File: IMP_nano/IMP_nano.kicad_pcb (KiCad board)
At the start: 2 copper layers, 34 parts, among them J1 KF301, J2 Holes, Q1 BC847, Q2 AO3400A, SW1 SW_DPST_x2, SW2 SW_DIP_x04, U1 STM32L051C8T6

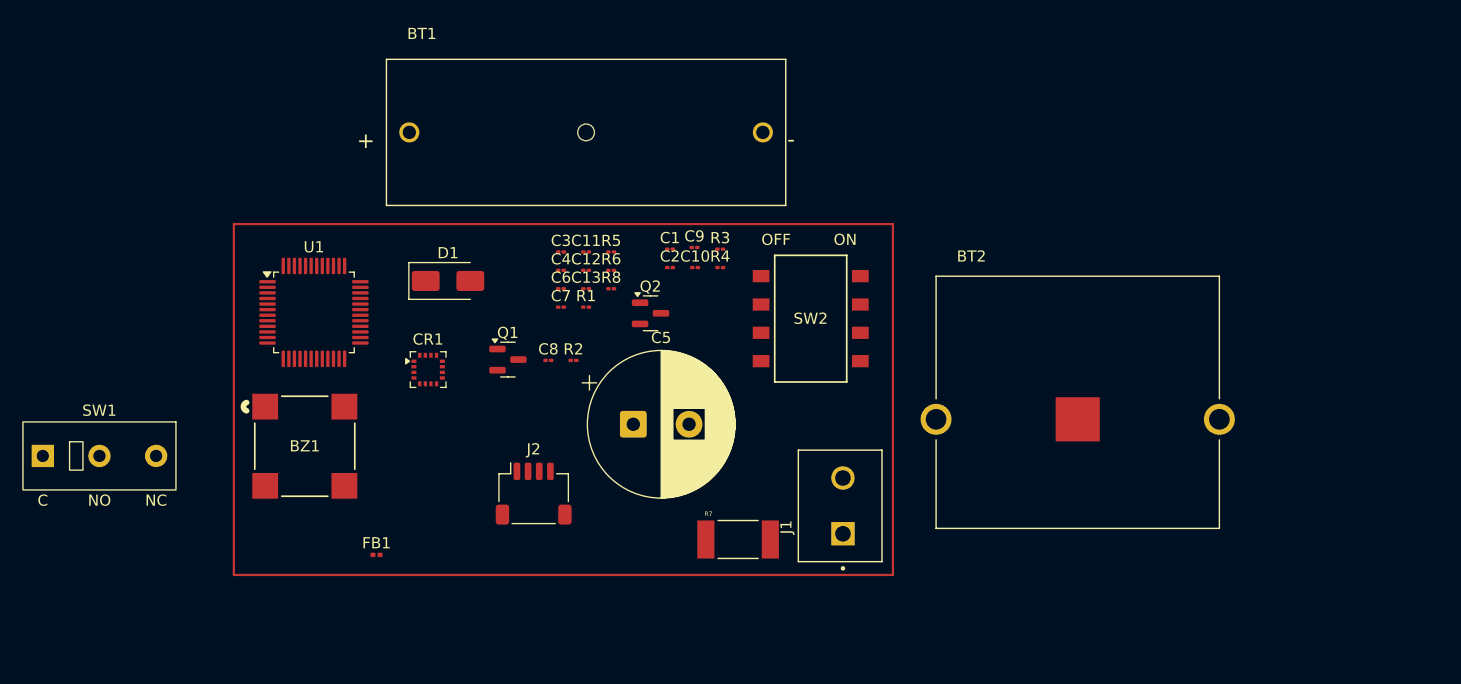
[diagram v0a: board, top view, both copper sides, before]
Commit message: precomplete of back side of pcb
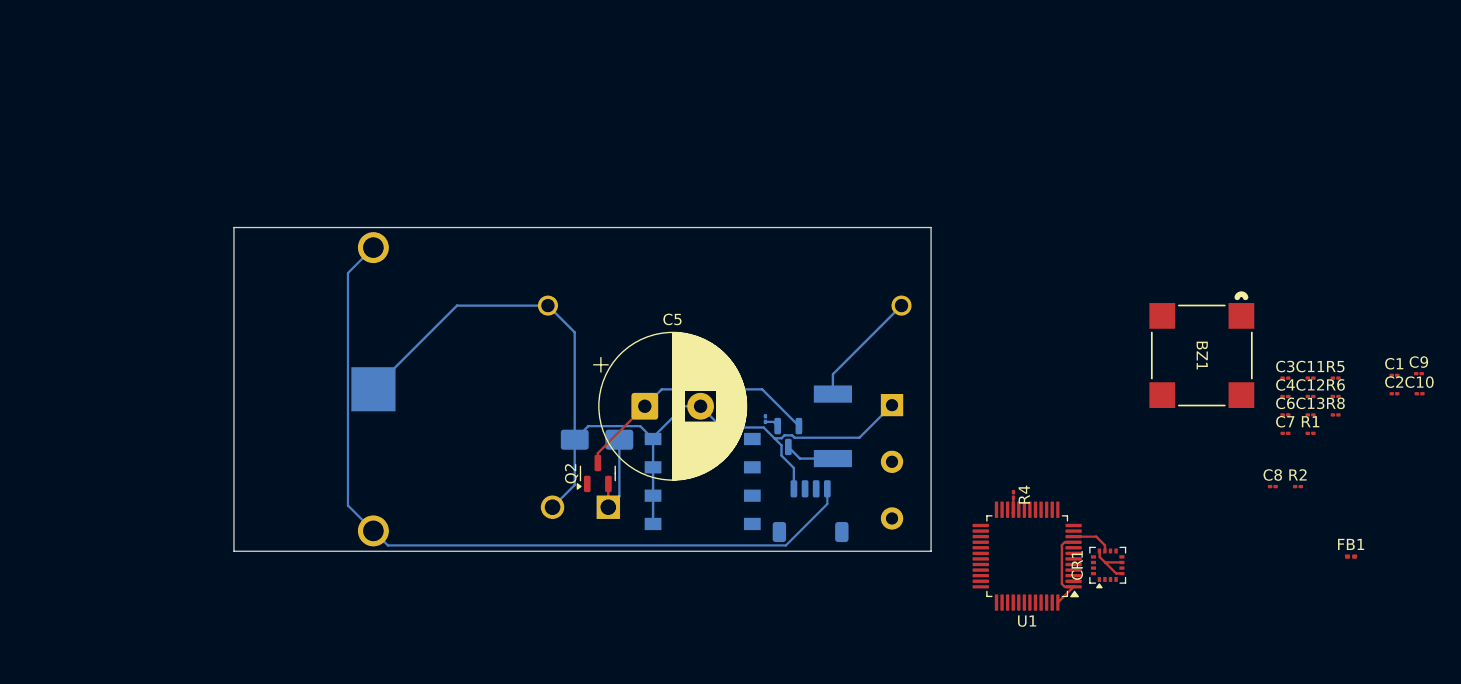
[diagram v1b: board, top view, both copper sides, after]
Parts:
- BT1, BT2, D1, J1, J2, Q1, R3, R7, SW1, SW2: moved to B.Cu
- moved FB1 87.4 mm to (193.7, 106.0)
- moved BZ1 80.8 mm to (180.3, 88.0), turned to -90 degrees
- moved SW1 76.3 mm to (152.5, 92.4), turned to -90 degrees
- moved U1 67.6 mm to (164.6, 106.0), turned to 180 degrees
- moved C1 65.9 mm to (197.6, 89.8)
- moved C10 65.9 mm to (199.8, 91.4)
- moved C11 65.9 mm to (190.0, 90.0)
- moved C12 65.9 mm to (190.0, 91.7)
- moved C13 65.9 mm to (190.0, 93.3)
- moved C2 65.9 mm to (197.6, 91.4)
- moved C3 65.9 mm to (187.8, 90.0)
- moved C4 65.9 mm to (187.8, 91.7)
- moved C6 65.9 mm to (187.8, 93.3)
- moved C7 65.9 mm to (187.8, 95.0)
- moved C8 65.9 mm to (186.6, 99.7)
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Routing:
- net GND: track 0.00 -> 89.6 mm
- net +3.3V: track 0.00 -> 79.2 mm
- net Net-(Q1-E): track 0.00 -> 22.6 mm
- net +12V: track 0.00 -> 10.5 mm
- net Net-(D1-K): track 0.00 -> 8.17 mm
- net Net-(Q1-C): track 0.00 -> 4.43 mm
- net GPIO_WKP: track 0.00 -> 3.64 mm
- net Activate: track 0.00 -> 1.50 mm
- net Net-(Q1-B): track 0.00 -> 1.26 mm
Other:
- board outline added: 62.5 x 29 mm

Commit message: PCB - placed all components - added filled copper zones(back - GND, front - 3v3)   SCHEMATIC - corrected mode switch
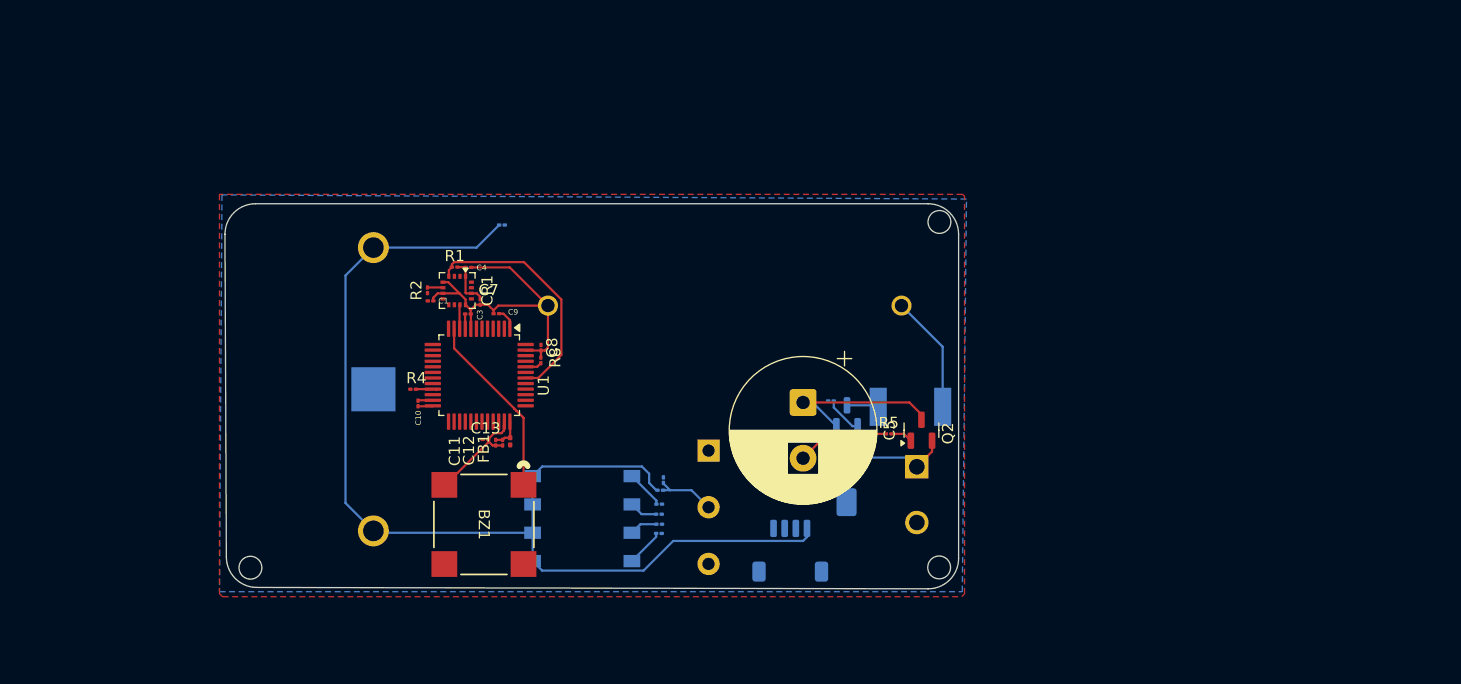
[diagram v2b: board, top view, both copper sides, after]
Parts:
- added R10: 10k, Resistor_SMD:R_01005_0402Metric, B.Cu at (131.6, 103.1)
- added R11: 10k, Resistor_SMD:R_01005_0402Metric, B.Cu at (131.6, 102.2)
- added R12: 10k, Resistor_SMD:R_01005_0402Metric, B.Cu at (131.6, 101.3)
- added R9: 10k, Resistor_SMD:R_01005_0402Metric, B.Cu at (131.6, 103.9)
- C2, C6, R6: moved to B.Cu
- moved C10 89.8 mm to (110.0, 92.3), turned to 90 degrees
- moved C1 86.7 mm to (111.1, 83.1)
- moved C9 82.9 mm to (117.0, 84.2), turned to 180 degrees
- moved R2 80.0 mm to (110.8, 82.1), turned to 90 degrees
- moved R1 78.2 mm to (113.3, 80.0)
- moved FB1 76.1 mm to (118.3, 95.7), turned to 90 degrees
- moved C4 74.2 mm to (114.5, 80.1)
- moved C7 74.1 mm to (114.5, 84.2)
- moved C13 74.0 mm to (116.0, 95.5)
- moved C11 73.3 mm to (117.0, 95.8), turned to -90 degrees
- moved C12 72.6 mm to (117.6, 95.8), turned to -90 degrees
- moved C3 72.5 mm to (115.6, 83.2), turned to -90 degrees
- moved C6 72.3 mm to (117.5, 76.3)
- moved R8 71.4 mm to (121.0, 88.4), turned to 90 degrees
- moved C8 66.8 mm to (121.0, 87.3), turned to -90 degrees
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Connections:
- SW2 pad 5: GND -> +3.3V
- SW2 pad 6: GND -> +3.3V
- SW2 pad 7: GND -> +3.3V
- SW2 pad 8: GND -> +3.3V
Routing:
- net GND: track 89.6 -> 50.7 mm
- net +3.3V: track 79.2 -> 111.0 mm
- net I2C_SCL: track 0.00 -> 21.5 mm
- net BUZ_PWM: track 0.00 -> 16.6 mm
- net Net-(Q1-E): track 22.6 -> 15.4 mm
- net NRST: track 0.00 -> 5.59 mm
- net PB12: track 0.00 -> 3.43 mm
- net PB15: track 0.00 -> 3.38 mm
- net +3.3VA: track 0.00 -> 3.01 mm
- net PB13: track 0.00 -> 2.54 mm
- net PB14: track 0.00 -> 2.52 mm
- net Net-(Q1-B): track 1.26 -> 3.41 mm
- net Net-(Q2-G): track 0.00 -> 1.99 mm
- net Net-(Q1-C): track 4.43 -> 2.85 mm
- net BOOT0: track 0.00 -> 1.50 mm
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- added copper zone on F.Cu, net +3.3V
- added copper zone on B.Cu, net GND
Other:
- board size 62.5 x 29 mm -> 65.8 x 34.5 mm

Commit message: update pcb & schematic
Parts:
- C5, Q2, R5: moved to B.Cu
- J1, R10, R11, R12, R9, SW2: moved to F.Cu
- moved R12 39.2 mm to (98.8, 79.9), turned to -90 degrees
- moved R11 39.0 mm to (99.7, 79.9), turned to -90 degrees
- moved R10 38.8 mm to (100.6, 79.9), turned to -90 degrees
- moved R9 38.6 mm to (101.4, 79.9), turned to -90 degrees
- moved SW2 25.0 mm to (100.3, 97.0)
- moved Q2 23.3 mm to (131.9, 92.5), turned to 180 degrees
- moved BZ1 23.1 mm to (100.3, 86.0), turned to 180 degrees
- moved C5 18.7 mm to (126.5, 97.0)
- moved R5 18.5 mm to (134.2, 90.7), turned to 180 degrees
- moved C2 4.70 mm to (132.5, 103.8), turned to 90 degrees
- moved R6 4.07 mm to (133.1, 103.9), turned to 90 degrees
- moved R7 1.62 mm to (152.5, 92.6)
- moved Q1 1.56 mm to (146.9, 93.4)
- moved R3 1.35 mm to (145.7, 92.0)
- moved J1 0.74 mm to (154.1, 100.9)
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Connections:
- net +12V renamed /12v
- net BOOT0 renamed /BOOT0
- net BUZ_PWM renamed /BUZ_PWM
- net GPIO_WKP renamed /GPIO_WKP
- net I2C_SCL renamed /I2C_SCL
- net I2C_SDA renamed /I2C_SDA
- net Net-(D1-K) renamed /12v_OUT
- net Net-(Q1-C) renamed /12v_R7
- net Net-(Q1-E) renamed /12v_C5
- R10 pad 2: PB14 -> /M_PB13
- R11 pad 2: PB13 -> /M_PB14
- R12 pad 2: PB12 -> /M_PB15
- R9 pad 2: PB15 -> /M_PB12
- SW2 pad 1: PB12 -> /M_PB15
- SW2 pad 2: PB13 -> /M_PB14
- SW2 pad 3: PB14 -> /M_PB13
- SW2 pad 4: PB15 -> /M_PB12
- U1 pad 25: PB12 -> /M_PB12
- U1 pad 26: PB13 -> /M_PB13
- U1 pad 27: PB14 -> /M_PB14
- U1 pad 28: PB15 -> /M_PB15
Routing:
- net /M_PB15: track 0.00 -> 36.1 mm
- net /SWDIO: track 0.00 -> 33.1 mm, vias 0 -> 1
- net /M_PB14: track 0.00 -> 31.6 mm
- net /SWCLK: track 0.00 -> 29.7 mm, vias 0 -> 1
- net /M_PB13: track 0.00 -> 27.1 mm
- net /M_PB12: track 0.00 -> 23.1 mm
- net GND: track 50.7 -> 72.6 mm
- net /12v_C5: track 15.4 -> 0.00 mm
- net /I2C_SDA: track 1.40 -> 15.0 mm, vias 0 -> 2
- net +3.3V: track 111.0 -> 99.8 mm
- net /12v: track 10.6 -> 0.00 mm
- net /BUZ_PWM: track 16.6 -> 12.3 mm
- net PB12: track 3.43 -> 0.00 mm
- net Net-(Q1-B): track 3.41 -> 0.00 mm
- net PB15: track 3.38 -> 0.00 mm
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
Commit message: fully made pcb & update schematic
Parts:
- C1, C10, C11, C12, C13, C2, C3, C4, C6, C7, C8, C9: footprint Capacitor_SMD:C_01005_0402Metric -> Capacitor_SMD:C_0201_0603Metric
- J1: moved to B.Cu
- R1, R10, R11, R12, R2, R3, R4, R5, R8, R9: footprint Resistor_SMD:R_01005_0402Metric -> Resistor_SMD:R_0201_0603Metric
- R6: footprint Resistor_SMD:R_01005_0402Metric -> Resistor_SMD:R_0201_0603Metric; moved to F.Cu
- SW1: moved to F.Cu
- moved J2 21.1 mm to (123.0, 102.0)
- moved C6 15.1 mm to (121.9, 90.8)
- moved R5 14.2 mm to (147.2, 96.4), turned to 90 degrees
- moved Q2 13.4 mm to (144.9, 95.7), turned to 90 degrees
- moved R6 11.6 mm to (123.7, 97.1), turned to -90 degrees
- moved C2 11.1 mm to (123.7, 97.0), turned to -90 degrees
- moved SW1 10.5 mm to (128.2, 102.6), turned to 90 degrees
- moved C5 9.63 mm to (135.8, 94.5)
- moved D1 3.26 mm to (145.8, 102.2)
- moved J1 2.60 mm to (151.9, 99.5)
- moved R3 2.37 mm to (143.7, 90.7)
- moved Q1 2.05 mm to (145.3, 92.0), turned to 180 degrees
- moved FB1 1.73 mm to (116.5, 95.9), turned to -90 degrees
- moved C11 1.04 mm to (118.0, 95.9), turned to 90 degrees
- moved R7 0.98 mm to (151.6, 92.2)
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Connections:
- net Activate renamed /Activate
- net Charge renamed /Charge
- net NRST renamed /NRST
- net Net-(Q1-B) renamed /Q1_1
- net Net-(Q2-G) renamed /Q2_1
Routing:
- net /Q2_1: track 1.54 -> 56.1 mm, vias 0 -> 1
- net +3.3V: track 99.8 -> 71.5 mm
- net /Charge: track 0.91 -> 27.7 mm, vias 0 -> 1
- net /SWDIO: track 33.1 -> 12.4 mm
- net /NRST: track 5.82 -> 23.4 mm
- net /SWCLK: track 29.7 -> 12.4 mm
- net /12v_C5: track 0.00 -> 13.2 mm
- net /12v: track 0.00 -> 9.22 mm
- net GND: track 72.6 -> 80.5 mm, vias 0 -> 3
- net /I2C_SDA: track 15.0 -> 20.8 mm
- net /12v_OUT: track 6.64 -> 11.6 mm
- net /I2C_SCL: track 21.5 -> 24.8 mm
- net /Q1_1: track 0.00 -> 2.40 mm
- net /12v_R7: track 3.41 -> 4.82 mm
- net +3.3VA: track 3.01 -> 4.14 mm
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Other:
- board size 65.8 x 34.5 mm -> 61.9 x 41.4 mm

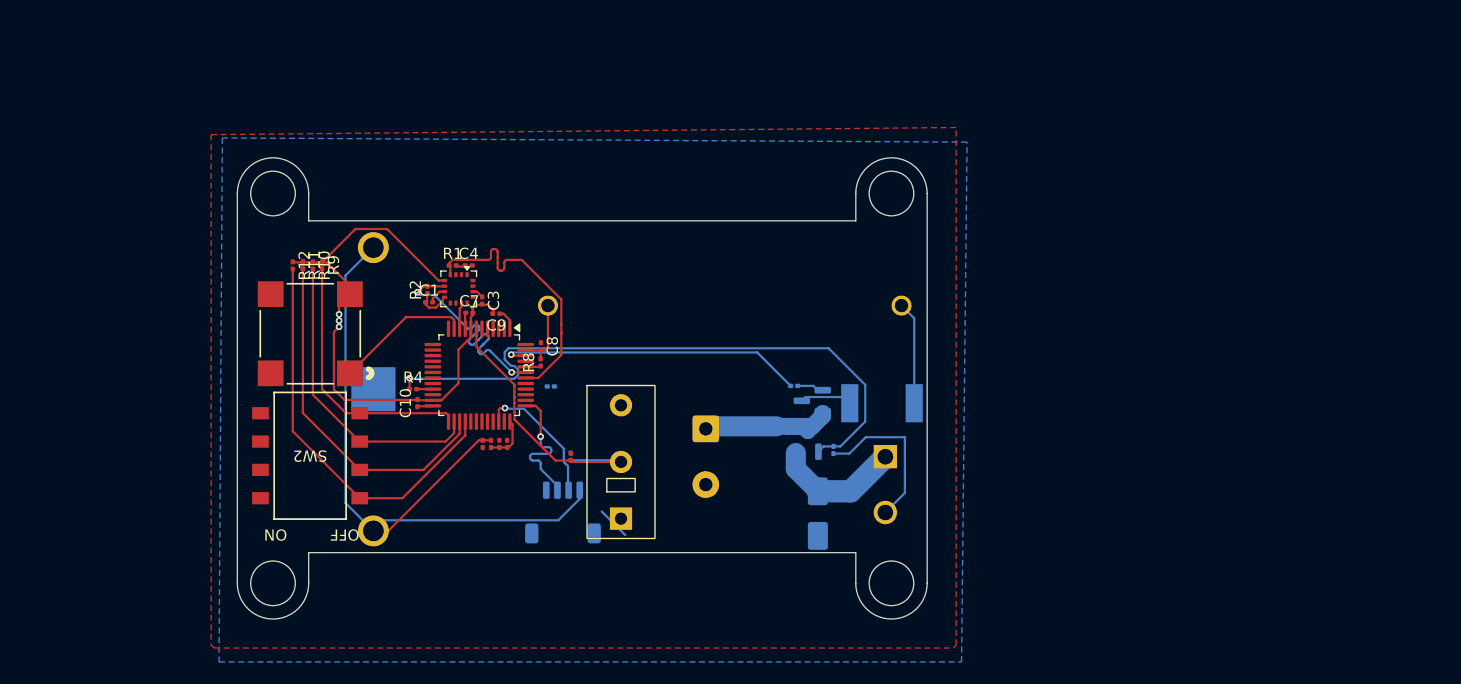
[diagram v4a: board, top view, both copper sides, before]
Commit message: No DRC errors on pcb
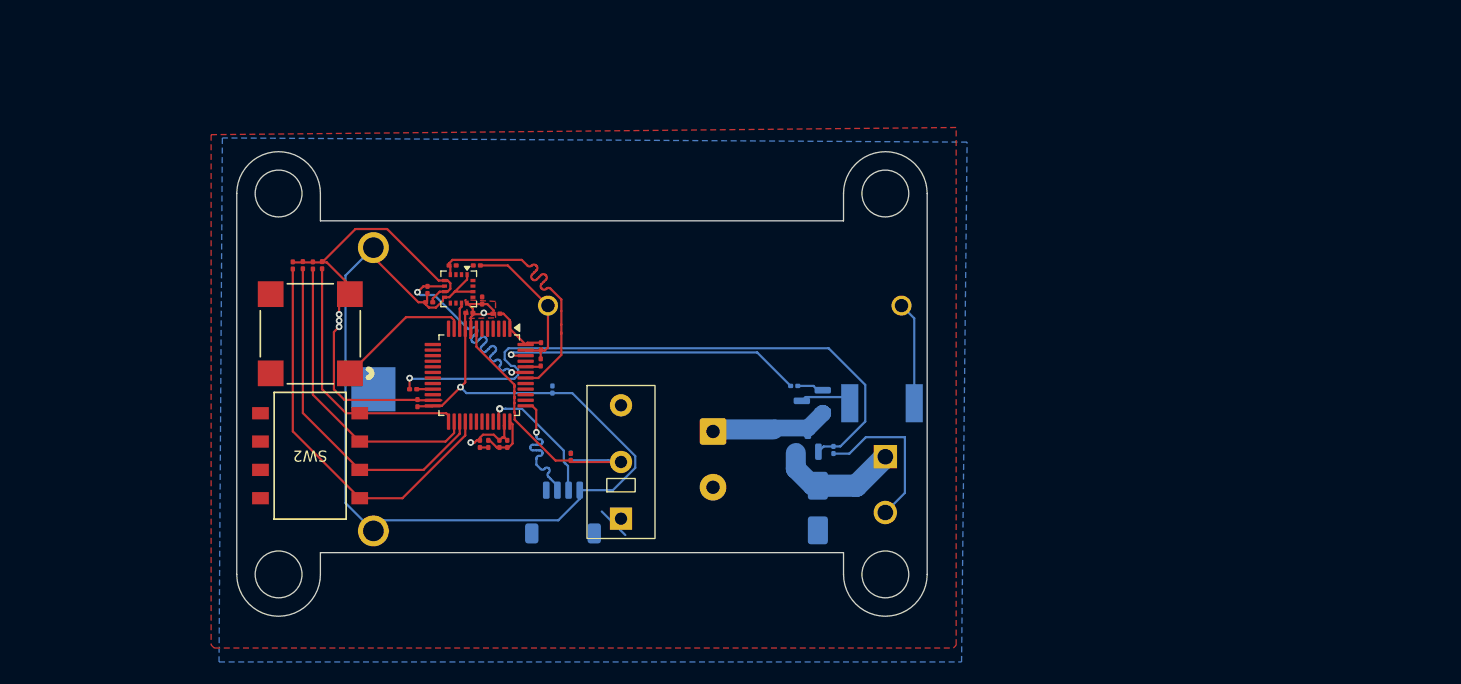
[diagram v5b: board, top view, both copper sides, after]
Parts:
- moved C4 0.73 mm to (115.3, 79.9)
- moved C5 0.69 mm to (136.4, 94.8)
- moved D1 0.50 mm to (145.8, 101.7)
- moved C6 0.31 mm to (122.0, 91.0), turned to 90 degrees
- moved C13 0.25 mm to (115.5, 95.9), turned to 90 degrees
- moved FB1 0.25 mm to (116.3, 95.9), turned to 90 degrees
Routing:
- net +3.3V: track 71.5 -> 106.9 mm, vias 0 -> 1
- net GND: track 80.5 -> 90.7 mm, vias 3 -> 5
- net /12v_C5: track 13.2 -> 10.5 mm
- net +3.3VA: track 4.14 -> 4.65 mm
- added copper zone on F.Cu, net GND
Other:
- board size 61.9 x 41.4 mm -> 61.9 x 41.6 mm

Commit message: Sigh and picture added to pcb
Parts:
- added G***: LOGO, IMP_LIB:DRAWING, F.Cu at (146.2, 82.1)
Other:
- board text added: "IMP_V0"

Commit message: corrected pcb & schematic
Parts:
- added R13: 120R, Resistor_SMD:R_0201_0603Metric, F.Cu at (106.1, 87.7)
- J2: value Holes -> SH1.04PIN
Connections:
- net /Q1_1 renamed Net-(Q1-B)
- net /Q2_1 renamed Net-(Q2-G)
- BZ1 pad 1: /BUZ_PWM -> Net-(BZ1-+)
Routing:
- net /BUZ_PWM: track 12.3 -> 9.02 mm
- net Net-(BZ1-+): track 0.00 -> 2.56 mm
